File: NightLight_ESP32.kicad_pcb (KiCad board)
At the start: 2 copper layers, 38.1 x 43.2 mm, 24 parts, among them J1 USB_OTG, J2 BUTTON, Q1 MMBT2222, Q2 MMBT2222, SW1 TL3342, SW2 TL3342, U1 ESP32-WROOM-32D, U2 AP2112K-3.3, U3 CP2104

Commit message: Fixed unconnected fills
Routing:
- net GND: track 33.3 -> 42.7 mm, vias 3 -> 7

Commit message: Tidy up of the silk screen
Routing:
- net +3V3: track 95.6 -> 97.9 mm
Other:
- board text added: "Button"
- board text added: "Reset"
- board text added: "SmartishNight"
- board text added: "v1"

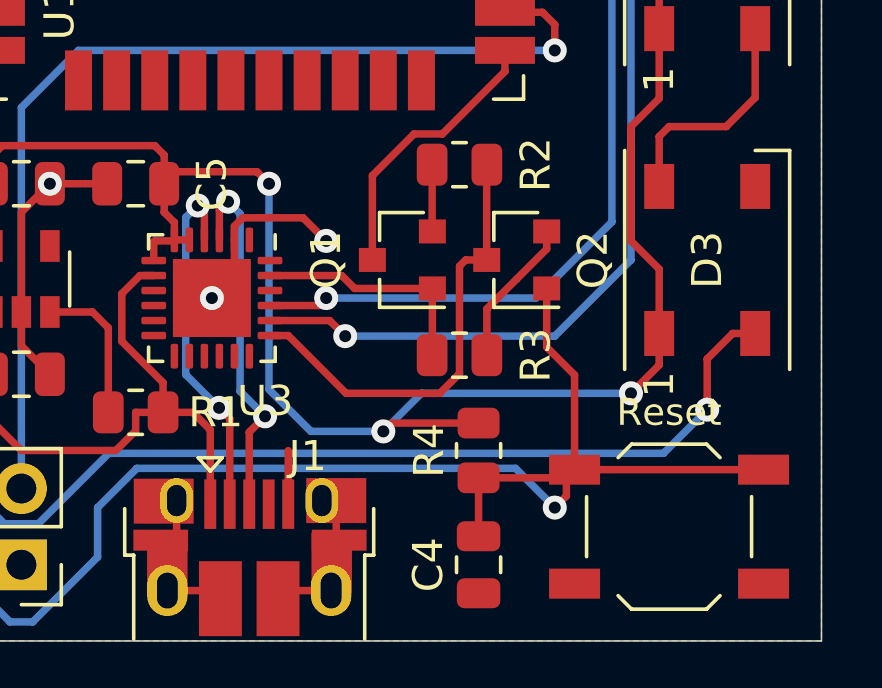
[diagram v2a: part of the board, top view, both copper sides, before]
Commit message: Fixed unconnected GND area
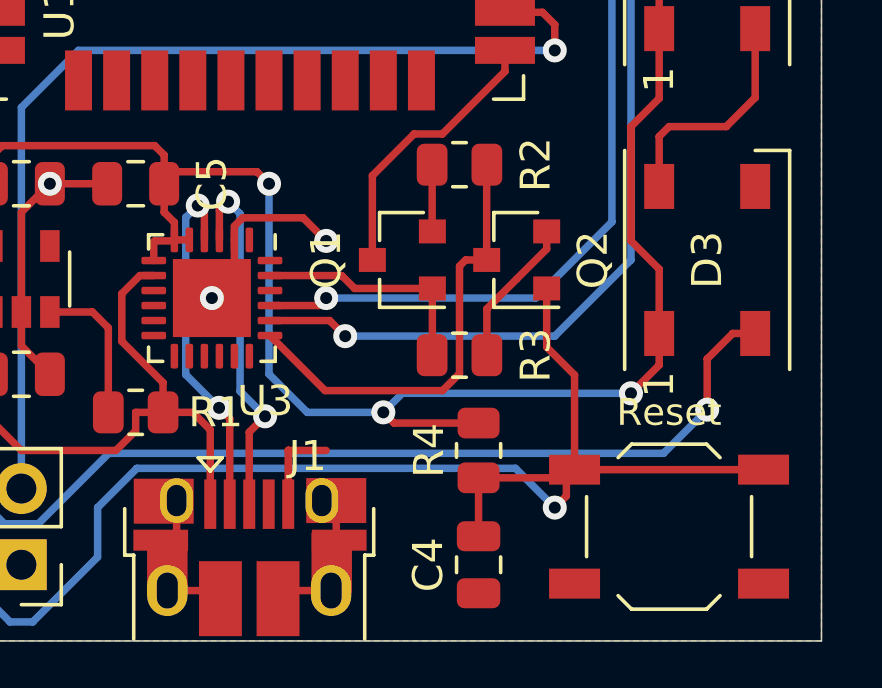
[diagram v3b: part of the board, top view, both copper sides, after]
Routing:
- net GND: track 42.7 -> 44.0 mm
- net +3V3: track 97.9 -> 97.1 mm
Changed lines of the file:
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@@
     (thickness 1.6)
     (drawings 10)
-    (tracks 256)
+    (tracks 258)
     (zones 0)
     (modules 24)
@@
   (segment (start 137.255 130.091) (end 136.945 130.401) (width 0.25) (layer F.Cu) (net 1))
   (segment (start 137.255 127.401) (end 137.255 130.091) (width 0.25) (layer F.Cu) (net 1))
-  (segment (start 140.975 127.521) (end 140.975 125.735) (width 0.25) (layer F.Cu) (net 1))
   (via (at 137.16 102.235) (size 0.8) (drill 0.4) (layers F.Cu B.Cu) (net 1))
   (segment (start 138.31 103.385) (end 137.16 102.235) (width 0.25) (layer F.Cu) (net 1))
@@
   (segment (start 139.185 103.385) (end 140.335 102.235) (width 0.25) (layer F.Cu) (net 1))
   (segment (start 138.7 103.385) (end 139.185 103.385) (width 0.25) (layer F.Cu) (net 1))
+  (segment (start 140.975 127.521) (end 140.975 125.725) (width 0.25) (layer F.Cu) (net 1))
+  (segment (start 140.975 125.725) (end 140.98 125.73) (width 0.25) (layer F.Cu) (net 1))
+  (segment (start 140.98 125.73) (end 142.24 125.73) (width 0.25) (layer F.Cu) (net 1))
   (segment (start 131.13 123.19) (end 131.13 121.115) (width 0.25) (layer F.Cu) (net 2))
   (segment (start 131.13 123.19) (end 131.13 124.78) (width 0.25) (layer F.Cu) (net 2))
@@
   (segment (start 140.335 116.84) (end 139.935001 116.440001) (width 0.25) (layer F.Cu) (net 3))
   (segment (start 139.935001 116.440001) (end 137.239999 116.440001) (width 0.25) (layer F.Cu) (net 3))
-  (via (at 144.145 125.095) (size 0.8) (drill 0.4) (layers F.Cu B.Cu) (net 3))
-  (segment (start 152.4 123.825) (end 145.415 123.825) (width 0.25) (layer B.Cu) (net 3))
-  (segment (start 147.32 124.8175) (end 144.4225 124.8175) (width 0.25) (layer F.Cu) (net 3))
-  (segment (start 144.4225 124.8175) (end 144.145 125.095) (width 0.25) (layer F.Cu) (net 3))
-  (segment (start 145.415 123.825) (end 144.145 125.095) (width 0.25) (layer B.Cu) (net 3))
-  (segment (start 140.335 123.698) (end 141.732 125.095) (width 0.25) (layer B.Cu) (net 3))
-  (segment (start 140.335 116.84) (end 140.335 123.698) (width 0.25) (layer B.Cu) (net 3))
-  (segment (start 141.732 125.095) (end 144.145 125.095) (width 0.25) (layer B.Cu) (net 3))
+  (via (at 144.145 124.459996) (size 0.8) (drill 0.4) (layers F.Cu B.Cu) (net 3))
+  (segment (start 144.779996 123.825) (end 144.145 124.459996) (width 0.25) (layer B.Cu) (net 3))
+  (segment (start 152.4 123.825) (end 144.779996 123.825) (width 0.25) (layer B.Cu) (net 3))
+  (segment (start 144.502504 124.8175) (end 144.145 124.459996) (width 0.25) (layer F.Cu) (net 3))
+  (segment (start 147.32 124.8175) (end 144.502504 124.8175) (width 0.25) (layer F.Cu) (net 3))
+  (segment (start 141.604996 124.459996) (end 144.145 124.459996) (width 0.25) (layer B.Cu) (net 3))
+  (segment (start 140.335 123.19) (end 141.604996 124.459996) (width 0.25) (layer B.Cu) (net 3))
+  (segment (start 140.335 116.84) (end 140.335 123.19) (width 0.25) (layer B.Cu) (net 3))
   (segment (start 149.59 122.285) (end 149.59 120.33) (width 0.25) (layer F.Cu) (net 4))
   (segment (start 150.52 123.215) (end 149.59 122.285) (width 0.25) (layer F.Cu) (net 4))
@@
   (segment (start 147.59 116.8475) (end 147.5975 116.84) (width 0.25) (layer F.Cu) (net 17))
   (segment (start 147.59 119.38) (end 147.59 116.8475) (width 0.25) (layer F.Cu) (net 17))
-  (segment (start 140.97625 121.9) (end 140.3675 121.9) (width 0.25) (layer F.Cu) (net 17))
-  (segment (start 146.02819 123.825) (end 142.90125 123.825) (width 0.25) (layer F.Cu) (net 17))
-  (segment (start 142.90125 123.825) (end 140.97625 121.9) (width 0.25) (layer F.Cu) (net 17))
-  (segment (start 146.685 123.16819) (end 146.02819 123.825) (width 0.25) (layer F.Cu) (net 17))
+  (segment (start 140.4925 122.025) (end 140.3675 121.9) (width 0.25) (layer F.Cu) (net 17))
+  (segment (start 142.202494 123.734994) (end 140.4925 122.025) (width 0.25) (layer F.Cu) (net 17))
+  (segment (start 146.118196 123.734994) (end 142.202494 123.734994) (width 0.25) (layer F.Cu) (net 17))
+  (segment (start 147.59 119.38) (end 146.89 119.38) (width 0.25) (layer F.Cu) (net 17))
   (segment (start 146.685 119.585) (end 146.685 123.16819) (width 0.25) (layer F.Cu) (net 17))
   (segment (start 146.89 119.38) (end 146.685 119.585) (width 0.25) (layer F.Cu) (net 17))
-  (segment (start 147.59 119.38) (end 146.89 119.38) (width 0.25) (layer F.Cu) (net 17))
+  (segment (start 146.685 123.16819) (end 146.118196 123.734994) (width 0.25) (layer F.Cu) (net 17))
   (segment (start 134.45 121.115) (end 133.03 121.115) (width 0.25) (layer F.Cu) (net 18))
   (segment (start 134.9775 121.6425) (end 134.45 121.115) (width 0.25) (layer F.Cu) (net 18))

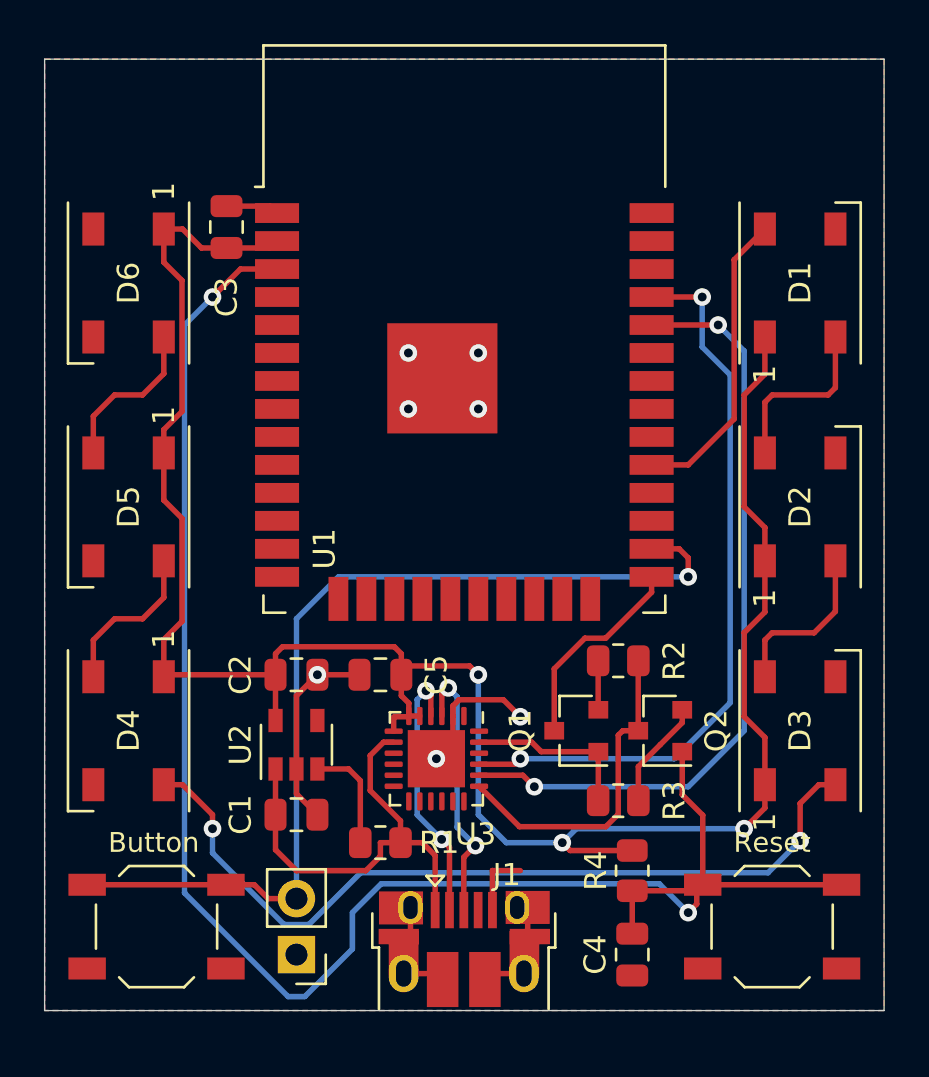
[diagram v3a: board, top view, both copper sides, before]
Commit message: Fixed issues with serial lines not being connected correctly
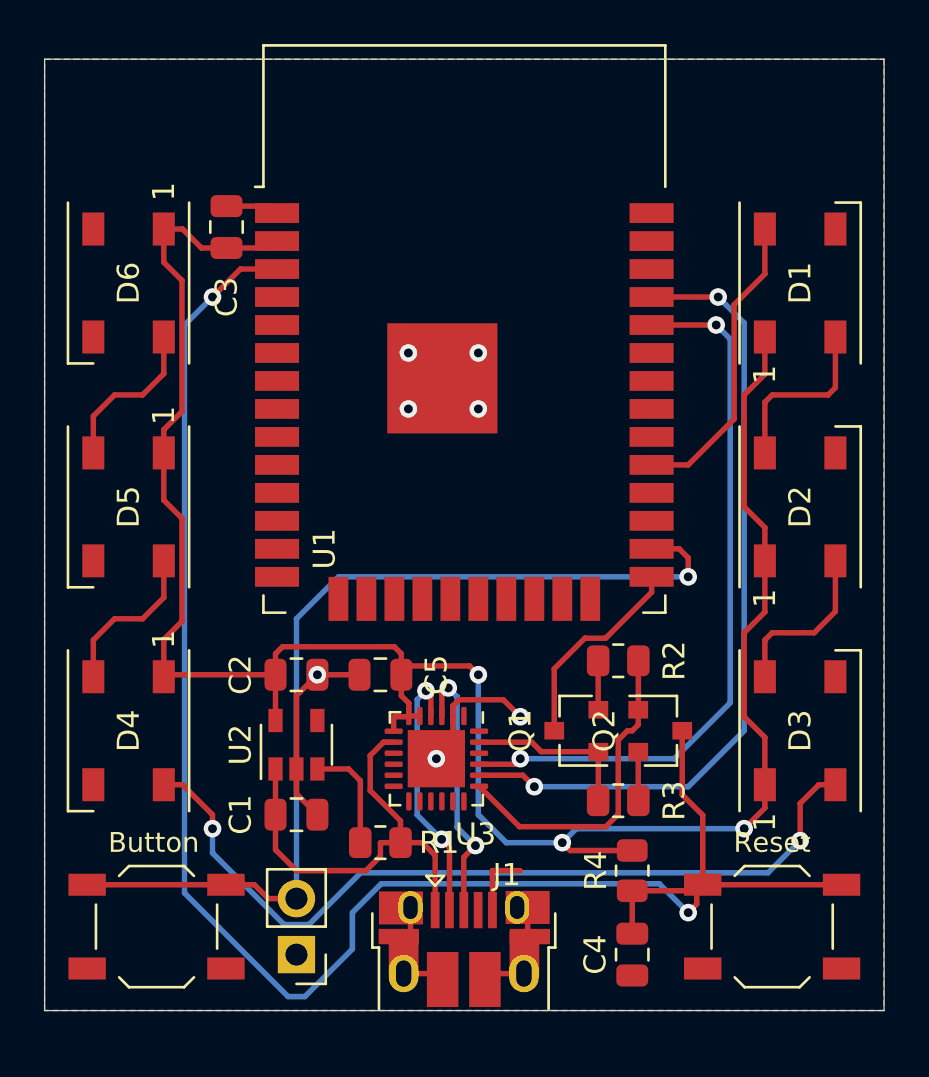
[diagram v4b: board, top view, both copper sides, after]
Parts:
- turned Q2 to 0 degrees
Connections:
- Q2 pad 1: /RESET -> /RTS
- Q2 pad 3: /RTS -> /RESET
- U1 pad 34: /RX -> /RXD0
- U1 pad 35: /TX -> /TXD0
- U3 pad 20: /RX -> /TXD0
- U3 pad 21: /TX -> /RXD0
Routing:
- net /TXD0: track 0.00 -> 36.5 mm, vias 0 -> 2
- net /RX: track 35.2 -> 0.00 mm, vias 2 -> 0
- net /TX: track 33.8 -> 0.00 mm, vias 2 -> 0
- net /RXD0: track 0.00 -> 32.9 mm, vias 0 -> 2
- net Net-(Q2-Pad2): track 4.32 -> 2.23 mm
- net /RESET: track 78.6 -> 79.6 mm

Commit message: Updated LEDs power to be configurable from 5V or 3.3V
Should be ok with a small circuot like this but close to the limits
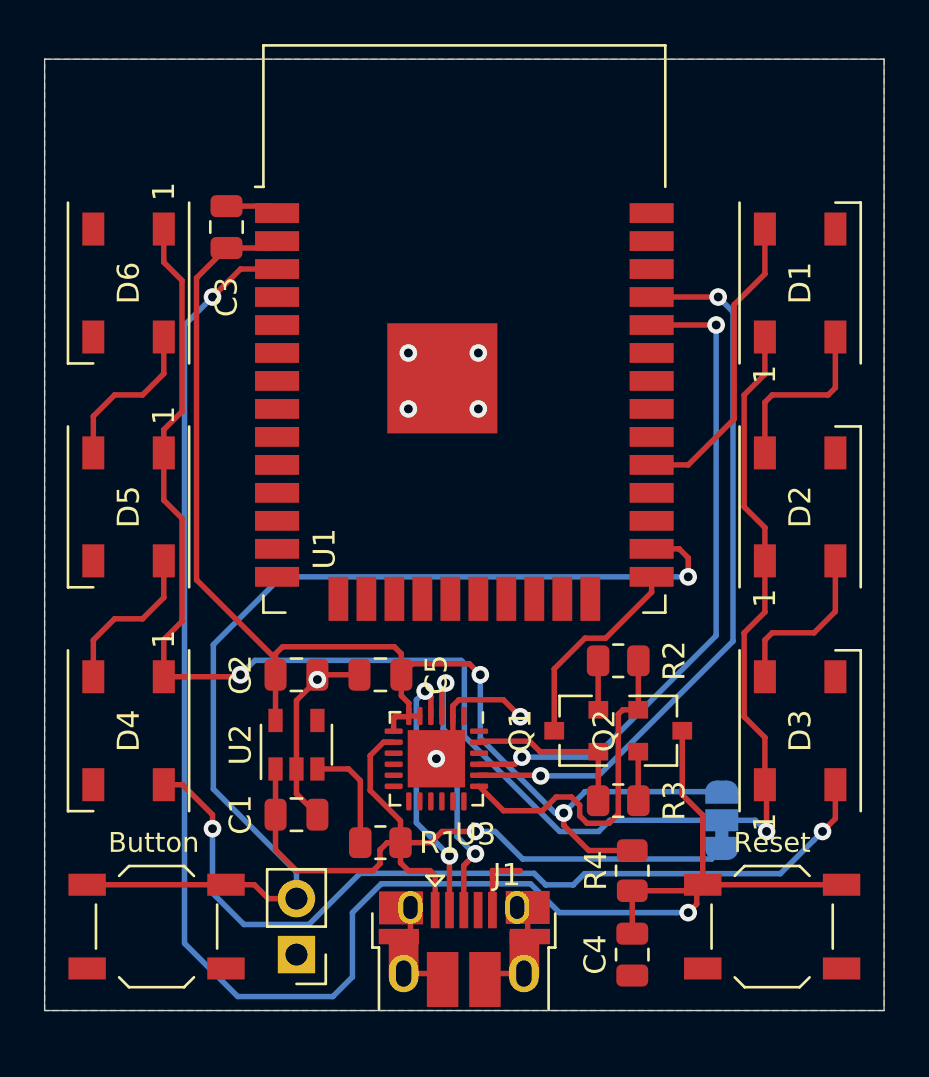
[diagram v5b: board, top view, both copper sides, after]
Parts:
- added JP1: SolderJumper_3_Bridged12, Jumper:SolderJumper-3_P1.3mm_Bridged12_RoundedPad1.0x1.5mm, B.Cu at (151.4, 123.4)
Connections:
- D1 pad 1: +3V3 -> /LED_POWER
- D2 pad 1: +3V3 -> /LED_POWER
- D3 pad 1: +3V3 -> /LED_POWER
- D4 pad 1: +3V3 -> /LED_POWER
- D5 pad 1: +3V3 -> /LED_POWER
- D6 pad 1: +3V3 -> /LED_POWER
- D6 pad 2: (no net) -> Net-(D6-Pad2)
- J1 pad 4: (no net) -> Net-(J1-Pad4)
- U1 pad 10: (no net) -> Net-(U1-Pad10)
- U1 pad 11: (no net) -> Net-(U1-Pad11)
- U1 pad 12: (no net) -> Net-(U1-Pad12)
- U1 pad 13: (no net) -> Net-(U1-Pad13)
- U1 pad 14: (no net) -> Net-(U1-Pad14)
- U1 pad 16: (no net) -> Net-(U1-Pad16)
- U1 pad 17: (no net) -> Net-(U1-Pad17)
- U1 pad 18: (no net) -> Net-(U1-Pad18)
- U1 pad 19: (no net) -> Net-(U1-Pad19)
- U1 pad 20: (no net) -> Net-(U1-Pad20)
- U1 pad 21: (no net) -> Net-(U1-Pad21)
- U1 pad 22: (no net) -> Net-(U1-Pad22)
- U1 pad 23: (no net) -> Net-(U1-Pad23)
- U1 pad 24: (no net) -> Net-(U1-Pad24)
- U1 pad 27: (no net) -> Net-(U1-Pad27)
- U1 pad 28: (no net) -> Net-(U1-Pad28)
- U1 pad 30: (no net) -> Net-(U1-Pad30)
- U1 pad 31: (no net) -> Net-(U1-Pad31)
- U1 pad 32: (no net) -> Net-(U1-Pad32)
- U1 pad 33: (no net) -> Net-(U1-Pad33)
- U1 pad 36: (no net) -> Net-(U1-Pad36)
- U1 pad 37: (no net) -> Net-(U1-Pad37)
- U1 pad 4: (no net) -> Net-(U1-Pad4)
- U1 pad 5: (no net) -> Net-(U1-Pad5)
- U1 pad 6: (no net) -> Net-(U1-Pad6)
- U1 pad 7: (no net) -> Net-(U1-Pad7)
- U1 pad 8: (no net) -> Net-(U1-Pad8)
- U1 pad 9: (no net) -> Net-(U1-Pad9)
- U2 pad 4: (no net) -> Net-(U2-Pad4)
- U3 pad 1: (no net) -> Net-(U3-Pad1)
- U3 pad 10: (no net) -> Net-(U3-Pad10)
- U3 pad 11: (no net) -> Net-(U3-Pad11)
- U3 pad 12: (no net) -> Net-(U3-Pad12)
- U3 pad 13: (no net) -> Net-(U3-Pad13)
- U3 pad 14: (no net) -> Net-(U3-Pad14)
- U3 pad 15: (no net) -> Net-(U3-Pad15)
- U3 pad 16: (no net) -> Net-(U3-Pad16)
- U3 pad 17: (no net) -> Net-(U3-Pad17)
- U3 pad 18: (no net) -> Net-(U3-Pad18)
- U3 pad 22: (no net) -> Net-(U3-Pad22)
- U3 pad 24: (no net) -> Net-(U3-Pad24)
- U3 pad 9: (no net) -> Net-(U3-Pad9)
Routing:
- net /LED_POWER: track 0.00 -> 79.0 mm, vias 0 -> 2
- net +3V3: track 97.1 -> 61.7 mm, vias 3 -> 2
- net VBUS: track 20.7 -> 36.3 mm, vias 0 -> 1
- net /BUTTON: track 43.7 -> 48.4 mm
- net /TXD0: track 36.5 -> 33.0 mm
- net /RXD0: track 32.9 -> 30.2 mm
- net /RESET: track 79.6 -> 81.6 mm
- net Net-(D3-Pad2): track 37.7 -> 39.2 mm
- net /RTS: track 14.8 -> 15.7 mm
- net /D+: track 12.5 -> 13.0 mm

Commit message: Fixed unconneced gnounds and a few other bits of tidy up
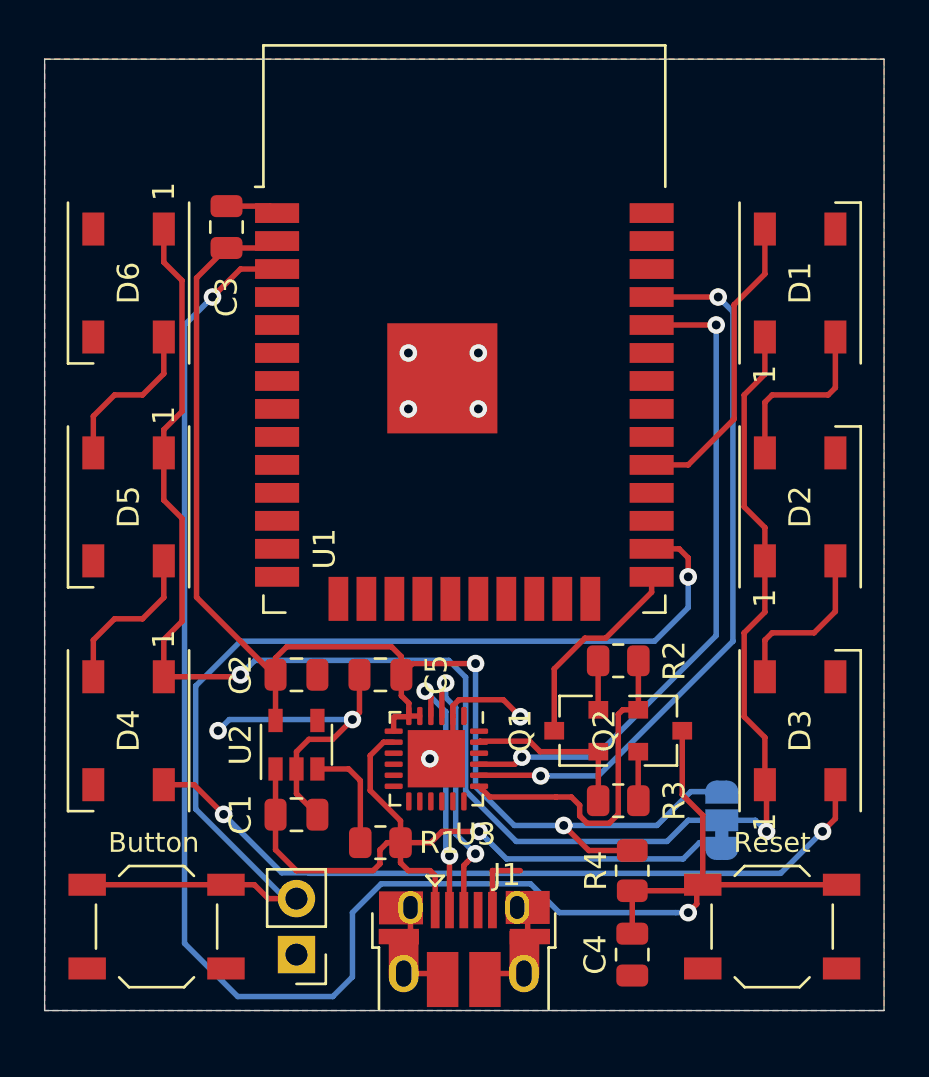
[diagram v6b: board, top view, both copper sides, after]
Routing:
- net GND: track 43.9 -> 49.9 mm, vias 7 -> 8
- net Net-(D3-Pad2): track 39.2 -> 34.7 mm
- net /LED_POWER: track 79.0 -> 80.4 mm
- net +3V3: track 61.7 -> 63.1 mm
- net /BUTTON: track 48.4 -> 49.5 mm
- net /RTS: track 15.7 -> 15.2 mm
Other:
- board text added: "3v"
- board text added: "5v"
- board text added: "LED Power"
- board text added: "v1.1"
- board text removed: "v1"
